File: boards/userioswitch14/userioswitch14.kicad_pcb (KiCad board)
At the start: 2 copper layers, 63 x 42 mm, 14 parts, among them IC1 SN3257QPWRQ1, IC2 SN3257QPWRQ1, J1 692112030100, J2 Conn_02x03_Odd_Even, J4 692122030100, J6 692122030100, J7 Header

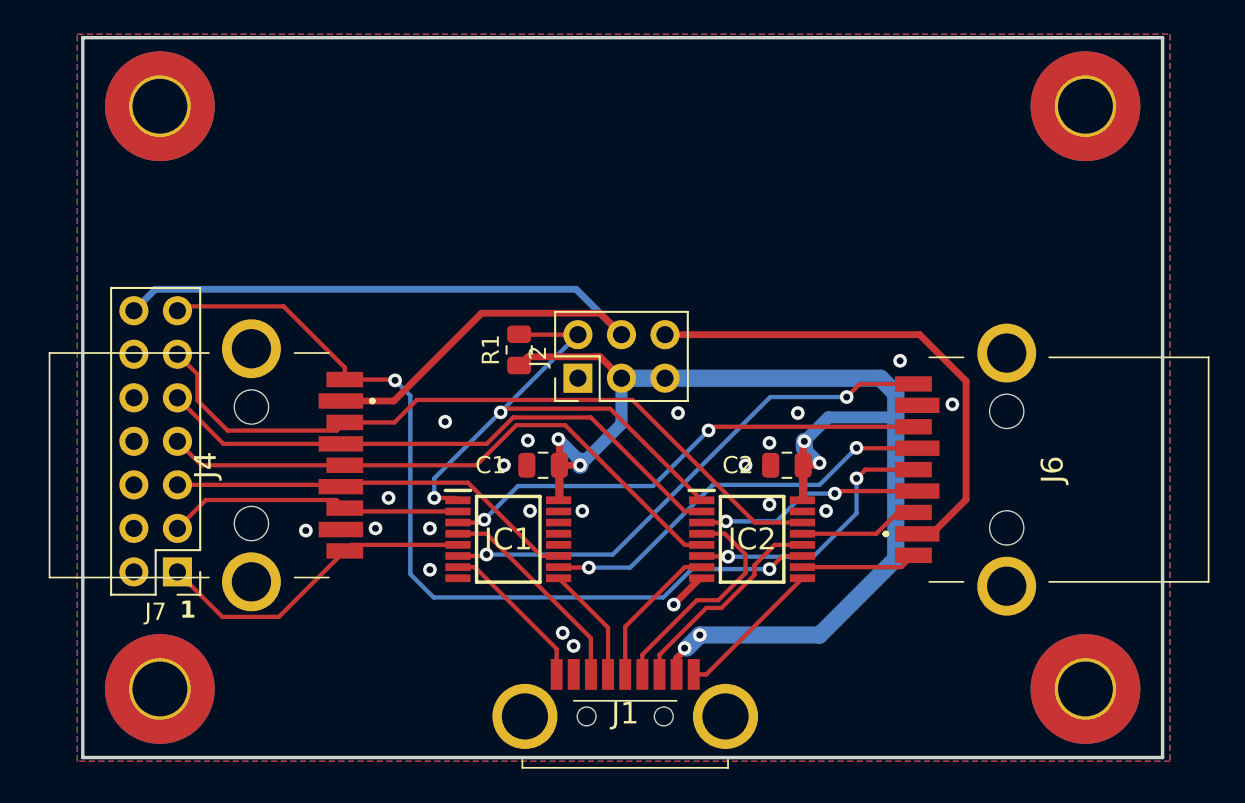
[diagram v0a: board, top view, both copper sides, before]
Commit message: Move to 14 pin headers for switch with off-board adapters
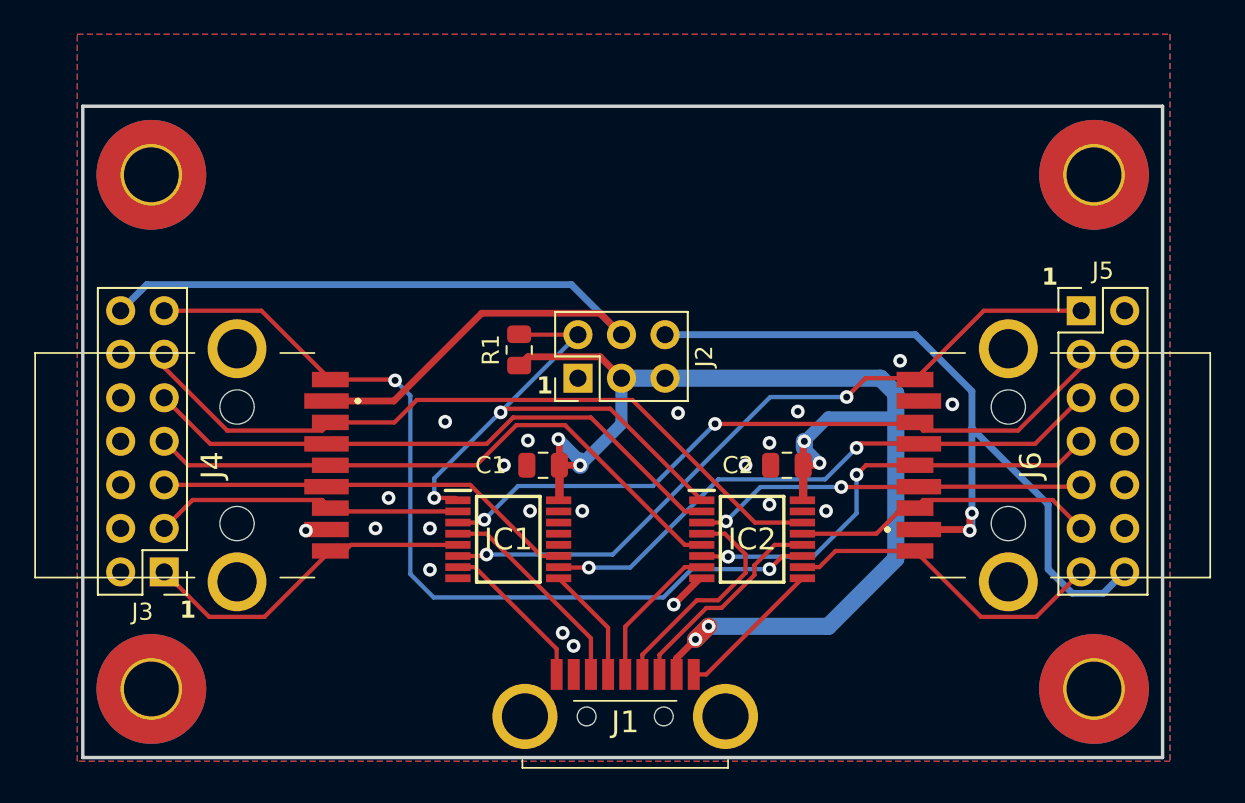
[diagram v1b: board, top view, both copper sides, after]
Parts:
- added J5: Header, Connector_PinHeader_2.54mm:PinHeader_2x07_P2.54mm_Vertical, F.Cu at (228.8, 82.9)
- H1, H2, H3, H4: value MountingHole_Pad -> M3
- J2: value Conn_02x03_Odd_Even -> 2x03
- moved H1 4.03 mm to (174.5, 75.0)
- moved H4 4.03 mm to (229.5, 75.0)
- moved J4 0.84 mm to (179.5, 91.9)
- moved J3 0.77 mm to (175.2, 98.2)
- moved H2 0.50 mm to (174.5, 105.0)
- moved H3 0.50 mm to (229.5, 105.0)
- moved J6 0.27 mm to (224.5, 91.9)
- renumbered J7 to J3
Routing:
- net /VBUSB: track 29.3 -> 47.0 mm, vias 0 -> 2
- net /S7B: track 6.76 -> 19.2 mm
- net /S4B: track 28.8 -> 41.1 mm
- net /S3B: track 30.7 -> 42.4 mm
- net /S2B: track 24.0 -> 34.6 mm
- net /S5B: track 15.7 -> 26.3 mm
- net /S6B: track 6.99 -> 17.6 mm
- net /S1B: track 13.2 -> 22.9 mm
- net VBUS: track 73.9 -> 74.9 mm
- net /VBUSA: track 49.1 -> 50.1 mm
- net /S7A: track 51.1 -> 50.4 mm
- net /S6A: track 42.9 -> 42.4 mm
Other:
- board size 63 x 42 mm -> 63 x 38 mm
